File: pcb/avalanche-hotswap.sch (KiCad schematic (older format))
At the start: 83 parts, among them J1 TRRS, SW1 SW_Push, SW10 SW_Push, SW11 SW_Push, SW12 SW_Push, SW13 SW_Push, SW14 SW_Push, SW15 SW_Push, SW16 SW_Push, SW17 SW_Push, SW18 SW_Push, SW19 SW_Push, SW2 SW_Push, SW20 SW_Push, SW21 SW_Push, SW22 SW_Push, SW23 SW_Push, SW24 SW_Push, SW25 SW_Push, SW26 SW_Push, SW27 SW_Push, SW28 SW_Push, SW29 SW_Push, SW3 SW_Push, SW30 SW_Push, SW31 SW_Push, SW32 SW_Push, SW4 SW_Push, SW5 SW_Push, SW6 SW_Push, SW7 SW_Push, SW8 SW_Push, SW9 SW_Push, U1 ProMicro

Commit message: Added to schema: * OLED * LED
Imported some footprints and symbols from Lily58
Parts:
- removed JP1, JP2, JP3, JP4: Jumper, used_footprints:Jumper_SMD, symbol Jumper:Jumper_2_Bridged
- added J2: LED, symbol 123_Lily58_Pro-cache:Lily58-cache_LED
- added J3: OLED, symbol 123_Lily58_Pro-cache:Lily58-cache_OLED
- added JP1, JP2, JP3, JP4, JP5, JP6, JP7, JP8: Device_Jumper_NO_Small, symbol 123_Lily58_Pro-cache:Device_Jumper_NO_Small
- added P1, P2: i2c_pin, symbol 123_Lily58_Pro-cache:Lily58-cache_i2c_pin
- added W1: jumper, symbol 123_Lily58_Pro-cache:Device_Jumper
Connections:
- net labels added: DATA, row0, row1, row2, row3, row4, row5
- net labels removed: rowA, rowB, rowC, rowD, rowE, rowF
- wire segments 88 -> 102
- no-connect marks 5 -> 3
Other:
- moved on the sheet: HM1, HM10, HM11, HM12, HM2, HM3, HM4, HM5, HM6, HM7, HM8, HM9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

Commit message: Moved all symbols to avalanche-hotswap.lib
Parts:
- J1: symbol avalanche-hotswap-rescue:MJ-4PP-9-kbd-Pcb-rescue-jiran-classic-rescue-jiran-hotswap-rescue-jiran-hotswap-rescue-thing60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 -> avalanche-hotswap:MJ-4PP-9
- J2: symbol 123_Lily58_Pro-cache:Lily58-cache_LED -> avalanche-hotswap:LED
- J3: symbol 123_Lily58_Pro-cache:Lily58-cache_OLED -> avalanche-hotswap:OLED
- JP1, JP2, JP3, JP4, JP5, JP6, JP7, JP8: symbol 123_Lily58_Pro-cache:Device_Jumper_NO_Small -> avalanche-hotswap:Device_Jumper_NO_Small
- P1, P2: symbol 123_Lily58_Pro-cache:Lily58-cache_i2c_pin -> avalanche-hotswap:i2c_pin
- U1: symbol avalanche-hotswap-rescue:ProMicro-kbd-Pcb-rescue-jiran-classic-rescue-jiran-hotswap-rescue-jiran-hotswap-rescue-thing60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 -> avalanche-hotswap:ProMicro_2
- W1: symbol 123_Lily58_Pro-cache:Device_Jumper -> avalanche-hotswap:Device_Jumper
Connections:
- net GND: now also J1.4; no longer J1.A
- net VCC: now also J1.1; no longer J1.D
- net at P2.1 (Pin_1), W1.2: now also J1.3; no longer J1.B
- net at P1.1 (Pin_1): now also J1.2; no longer J1.C
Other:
- moved on the sheet: P1, P2, R1, R2, W1

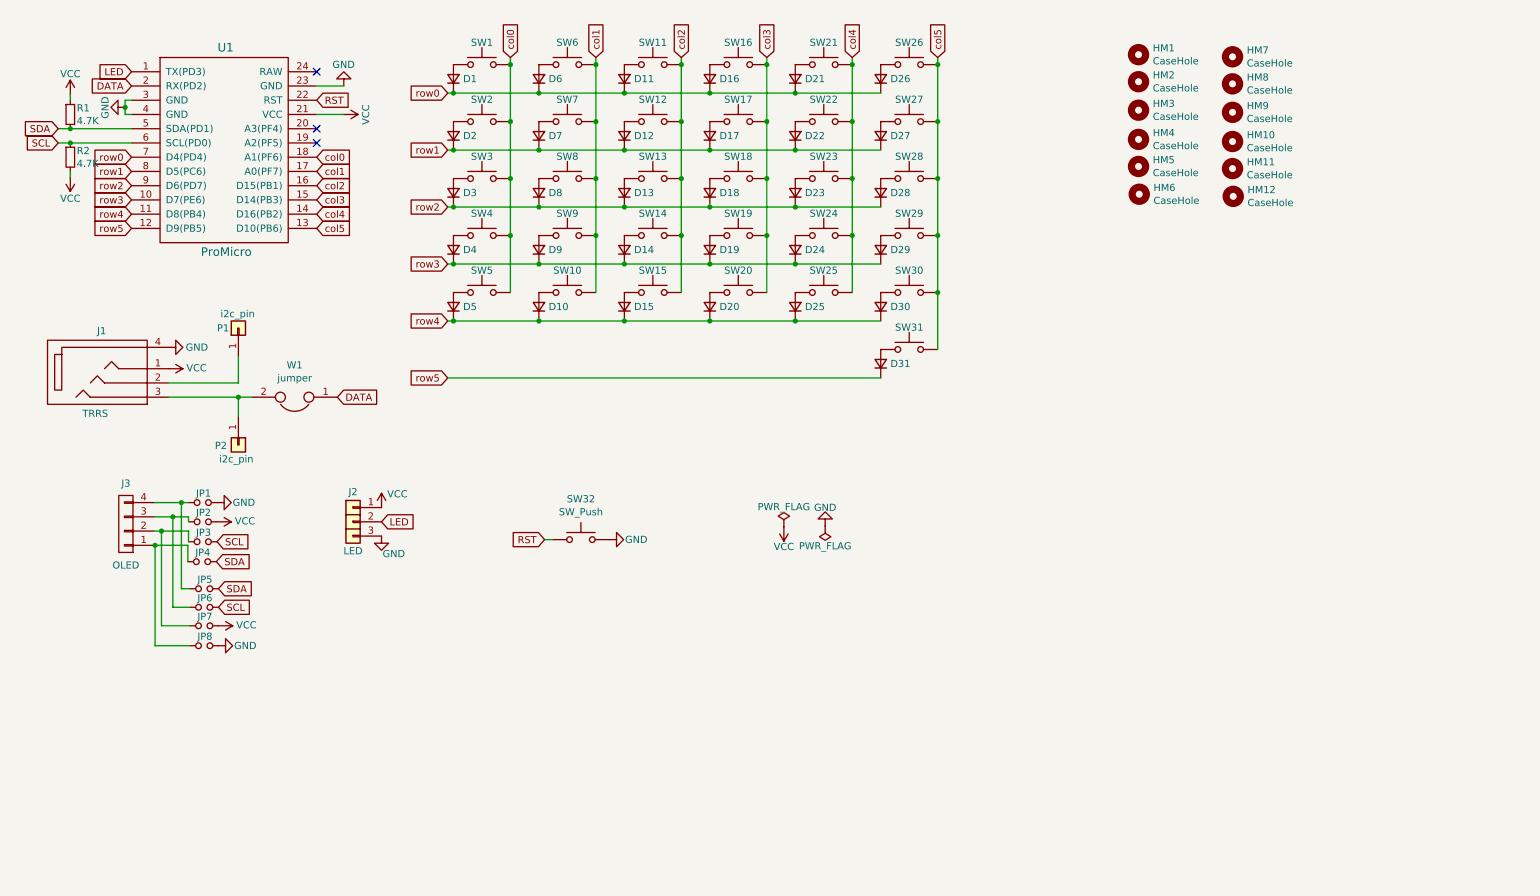
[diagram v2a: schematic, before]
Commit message: Added underglow LEDs and many more...
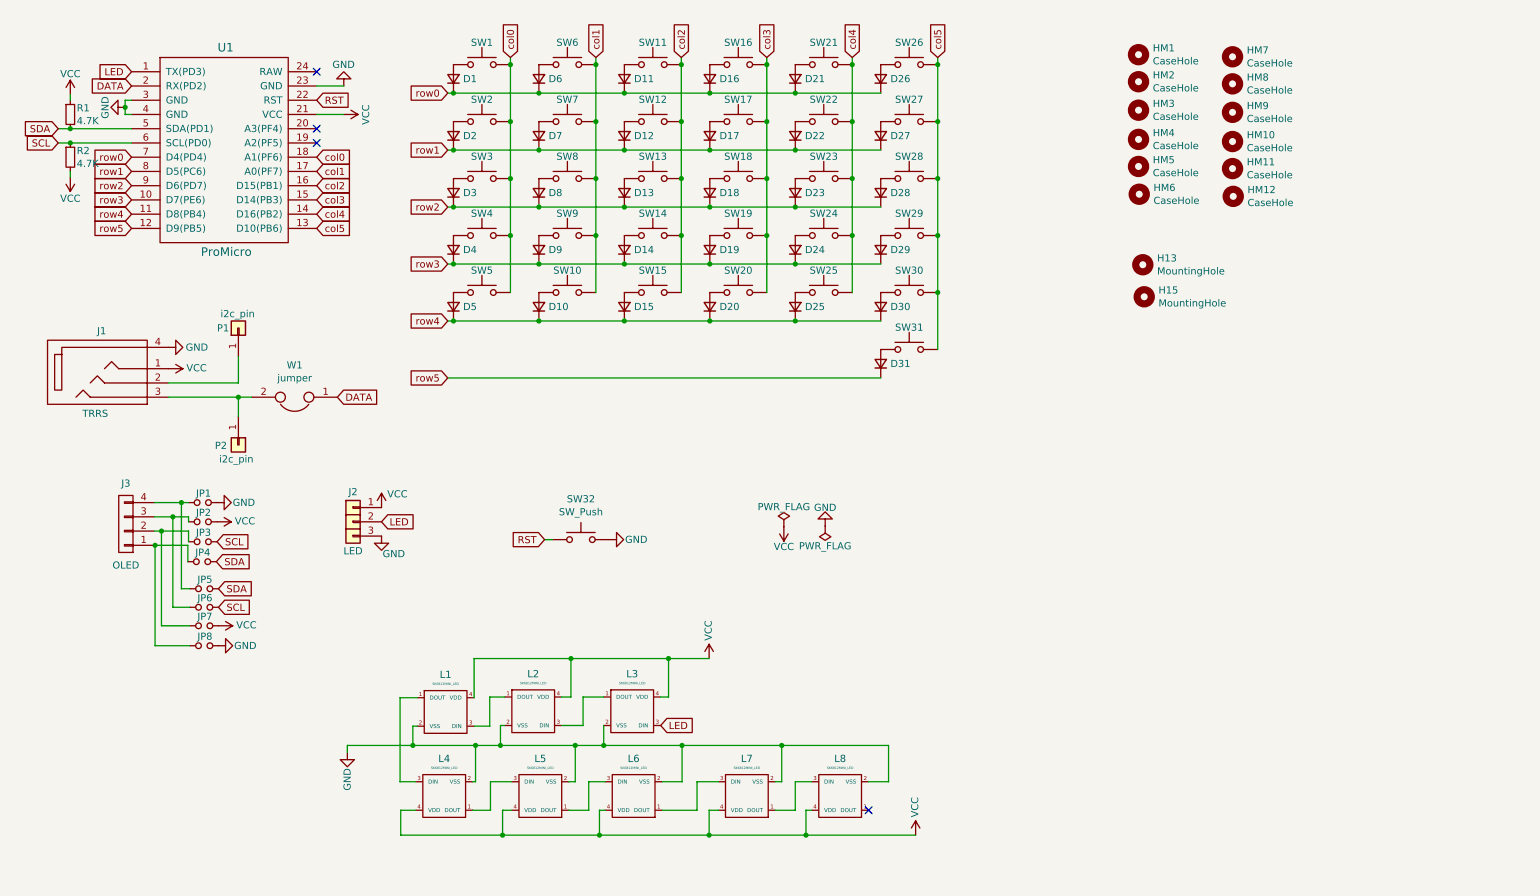
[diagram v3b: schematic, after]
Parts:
- added H13, H15: MountingHole, used_footprints:M2_HOLE_PCB, symbol Mechanical:MountingHole
- added L1, L2, L3, L4, L5, L6, L7, L8: SK6812MINI_LED, used_footprints:SK6812MINI_underglow_rev, symbol avalanche-hotswap:SK6812MINI_LED
- J1: footprint used_footprints:TRSS_DUAL_THT -> used_footprints:MJ-4PP-9
- J2: footprint (none) -> used_footprints:LED
- J3: footprint (none) -> used_footprints:OLED_4Pin
- JP1, JP2, JP3, JP4, JP5, JP6, JP7, JP8: footprint (none) -> used_footprints:avalanche_Jumper
- P1, P2: footprint (none) -> used_footprints:1pin_conn
- R1, R2: footprint used_footprints:Resistor_Hybrid_1205 -> used_footprints:RESISTOR_mini
- U1: footprint used_footprints:ProMicro_Dual -> used_footprints:ProMicro_rev2
- W1: footprint (none) -> used_footprints:jumper_data
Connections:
- net GND: now also L1.2 (VSS), L2.2 (VSS), L3.2 (VSS), L4.2 (VSS), L5.2 (VSS), L6.2 (VSS), L7.2 (VSS), L8.2 (VSS)
- net LED: now also L3.3 (DIN)
- net VCC: now also L1.4 (VDD), L2.4 (VDD), L3.4 (VDD), L4.4 (VDD), L5.4 (VDD), L6.4 (VDD), L7.4 (VDD), L8.4 (VDD)
- new net: L7.1 (DOUT), L8.3 (DIN)
- new net: L6.1 (DOUT), L7.3 (DIN)
- new net: L1.1 (DOUT), L4.3 (DIN)
- new net: L1.3 (DIN), L2.1 (DOUT)
- new net: L2.3 (DIN), L3.1 (DOUT)
- new net: L4.1 (DOUT), L5.3 (DIN)
- new net: L5.1 (DOUT), L6.3 (DIN)
- no-connect marks 3 -> 4

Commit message: WIP
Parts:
- added H16: MountingHole, used_footprints:M2_HOLE_PCB, symbol Mechanical:MountingHole
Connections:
- net at L7.1 (DOUT): now also L6.3 (DIN); no longer L8.3 (DIN)
- net at L7.3 (DIN): now also L8.1 (DOUT); no longer L6.1 (DOUT)
- net at L4.3 (DIN): now also L5.1 (DOUT); no longer L1.1 (DOUT)
- net at L4.1 (DOUT): no longer L5.3 (DIN)
- new net: L5.3 (DIN), L6.1 (DOUT)
- new net L_pin1_to_3: L1.1 (DOUT), L8.3 (DIN)
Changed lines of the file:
@@
 F 3 "" H 3480 6025 60  0001 C CNN
 	1    3480 6025
-	-1   0    0    1
+	1    0    0    -1
 $EndComp
 $Comp
@@
 F 3 "" H 4155 6025 60  0001 C CNN
 	1    4155 6025
-	-1   0    0    1
+	1    0    0    -1
 $EndComp
 $Comp
@@
 F 3 "" H 4810 6025 60  0001 C CNN
 	1    4810 6025
-	-1   0    0    1
+	1    0    0    -1
 $EndComp
 Text GLabel 5000 5530 2    50   Input ~ 0
 LED
 $Comp
-L power:VCC #PWR?
+L power:VCC #PWR0107
 U 1 1 6057DCAA
 P 5340 5060
-F 0 "#PWR?" H 5340 4910 50  0001 C CNN
+F 0 "#PWR0107" H 5340 4910 50  0001 C CNN
 F 1 "VCC" V 5335 5185 50  0000 L CNN
 F 2 "" H 5340 5060 50  0001 C CNN
@@
 	3800 5535 3690 5535
 Wire Wire Line
-	3290 5335 3170 5335
-Wire Wire Line
-	3170 5335 3170 5925
-Wire Wire Line
-	3170 5925 3280 5925
-Wire Wire Line
 	3955 5925 3805 5925
 Wire Wire Line
@@
 	4495 6125 4355 6125
 $Comp
-L power:GND #PWR?
+L power:GND #PWR0108
 U 1 1 605AF8A2
 P 2800 5720
-F 0 "#PWR?" H 2800 5470 50  0001 C CNN
+F 0 "#PWR0108" H 2800 5470 50  0001 C CNN
 F 1 "GND" V 2800 5610 50  0000 R CNN
 F 2 "" H 2800 5720 50  0001 C CNN
@@
 Connection ~ 3260 5670
 Wire Wire Line
-	3260 5670 3700 5670
-Wire Wire Line
 	3905 5530 3875 5530
 Wire Wire Line
@@
 Connection ~ 3875 5670
 Wire Wire Line
-	3875 5670 4400 5670
-Wire Wire Line
-	4600 5670 5150 5670
-Wire Wire Line
-	5150 5670 5150 5925
-Wire Wire Line
 	5150 5925 5010 5925
 Connection ~ 4600 5670
 Wire Wire Line
-	3280 6125 3175 6125
-Wire Wire Line
-	3175 6125 3175 6300
-Wire Wire Line
-	3175 6300 3890 6300
-Wire Wire Line
 	4610 6125 4570 6125
 Wire Wire Line
@@
 	3890 6300 4570 6300
 $Comp
-L power:VCC #PWR?
+L power:VCC #PWR0109
 U 1 1 6061C798
-P 6790 6300
-F 0 "#PWR?" H 6790 6150 50  0001 C CNN
-F 1 "VCC" V 6785 6425 50  0000 L CNN
-F 2 "" H 6790 6300 50  0001 C CNN
-F 3 "" H 6790 6300 50  0001 C CNN
-	1    6790 6300
+P 6990 5780
+F 0 "#PWR0109" H 6990 5630 50  0001 C CNN
+F 1 "VCC" V 6985 5905 50  0000 L CNN
+F 2 "" H 6990 5780 50  0001 C CNN
+F 3 "" H 6990 5780 50  0001 C CNN
+	1    6990 5780
 	1    0    0    -1
 $EndComp
@@
 	3680 5925 3700 5925
 Wire Wire Line
-	3700 5925 3700 5670
-Connection ~ 3700 5670
-Wire Wire Line
-	3700 5670 3875 5670
-Wire Wire Line
 	4355 5925 4400 5925
-Wire Wire Line
-	4400 5925 4400 5670
-Connection ~ 4400 5670
-Wire Wire Line
-	4400 5670 4600 5670
 $Comp
 L avalanche-hotswap:SK6812MINI_LED L7
@@
 F 3 "" H 5605 6025 60  0001 C CNN
 	1    5605 6025
-	-1   0    0    1
+	1    0    0    -1
 $EndComp
 $Comp
@@
 F 3 "" H 6260 6025 60  0001 C CNN
 	1    6260 6025
-	-1   0    0    1
+	1    0    0    -1
 $EndComp
 Wire Wire Line
@@
 	5945 6125 5805 6125
 Wire Wire Line
-	6600 5925 6460 5925
-Wire Wire Line
 	6060 6125 6020 6125
 Wire Wire Line
 	6020 6125 6020 6300
-Connection ~ 6020 6300
-Wire Wire Line
-	6020 6300 6790 6300
 Wire Wire Line
 	5405 6125 5340 6125
-NoConn ~ 6460 6125
 Wire Wire Line
 	5805 5925 5850 5925
-Wire Wire Line
-	5850 5925 5850 5670
 Wire Wire Line
 	4570 6300 5340 6300
@@
 Wire Wire Line
 	5340 6300 6020 6300
-Wire Wire Line
-	5850 5670 5150 5670
-Connection ~ 5150 5670
-Wire Wire Line
-	6600 5925 6600 5670
-Wire Wire Line
-	6600 5670 5850 5670
-Connection ~ 5850 5670
+$Comp
+L power:GND #PWR0110
+U 1 1 60493A43
+P 2715 6350
+F 0 "#PWR0110" H 2715 6100 50  0001 C CNN
+F 1 "GND" V 2715 6240 50  0000 R CNN
+F 2 "" H 2715 6350 50  0001 C CNN
+F 3 "" H 2715 6350 50  0001 C CNN
+	1    2715 6350
+	1    0    0    -1
+$EndComp
+Wire Wire Line
+	2715 6350 2715 6300
+Wire Wire Line
+	2715 6300 3170 6300
+Wire Wire Line
+	3260 5670 3875 5670
+Wire Wire Line
+	3875 5670 4600 5670
+Wire Wire Line
+	4600 5670 6600 5670
+Wire Wire Line
+	6460 5925 6535 5925
+Wire Wire Line
+	6535 5925 6535 5780
+Connection ~ 6535 5780
+Wire Wire Line
+	6535 5780 6990 5780
+Wire Wire Line
+	5850 5780 5850 5925
+Wire Wire Line
+	5850 5780 6535 5780
+Wire Wire Line
+	5850 5780 5150 5780
+Wire Wire Line
+	5150 5780 5150 5925
+Connection ~ 5850 5780
+Wire Wire Line
+	5150 5780 4400 5780
+Wire Wire Line
+	4400 5780 4400 5925
+Connection ~ 5150 5780
+Wire Wire Line
+	4400 5780 3700 5780
+Wire Wire Line
+	3700 5780 3700 5925
+Connection ~ 4400 5780
+Wire Wire Line
+	3280 6125 3170 6125
+Wire Wire Line
+	3170 6125 3170 6300
+Connection ~ 3170 6300
+Wire Wire Line
+	3170 6300 3890 6300
+NoConn ~ 3280 5925
+Text Label 3290 5335 2    50   ~ 0
+L_pin1_to_3
+Text Label 6460 6125 0    50   ~ 0
+L_pin1_to_3
+$Comp
+L Mechanical:MountingHole H16
+U 1 1 6044455C
+P 8415 2760
+F 0 "H16" H 8515 2806 50  0000 L CNN
+F 1 "MountingHole" H 8515 2715 50  0000 L CNN
+F 2 "used_footprints:M2_HOLE_PCB" H 8415 2760 50  0001 C CNN
+F 3 "~" H 8415 2760 50  0001 C CNN
+	1    8415 2760
+	1    0    0    -1
+$EndComp
 $EndSCHEMATC

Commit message: Routing...
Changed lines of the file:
@@
 Wire Wire Line
 	5150 5925 5010 5925
-Connection ~ 4600 5670
 Wire Wire Line
 	4610 6125 4570 6125
@@
 	3875 5670 4600 5670
 Wire Wire Line
-	4600 5670 6600 5670
-Wire Wire Line
 	6460 5925 6535 5925

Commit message: Routing...
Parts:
- renumbered L3 to L1, L1 to L3, L8 to L4, L7 to L5, L5 to L7, L4 to L8
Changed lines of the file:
@@
 $EndComp
 $Comp
-L avalanche-hotswap:SK6812MINI_LED L1
+L avalanche-hotswap:SK6812MINI_LED L3
 U 1 1 60550286
 P 3490 5435
-F 0 "L1" H 3490 5697 51  0000 C CNN
+F 0 "L3" H 3490 5697 51  0000 C CNN
 F 1 "SK6812MINI_LED" H 3490 5632 16  0000 C CNN
 F 2 "used_footprints:SK6812MINI_underglow_rev" H 3490 5435 60  0001 C CNN
@@
 $EndComp
 $Comp
-L avalanche-hotswap:SK6812MINI_LED L3
+L avalanche-hotswap:SK6812MINI_LED L1
 U 1 1 605637A3
 P 4800 5430
-F 0 "L3" H 4800 5692 51  0000 C CNN
+F 0 "L1" H 4800 5692 51  0000 C CNN
 F 1 "SK6812MINI_LED" H 4800 5627 16  0000 C CNN
 F 2 "used_footprints:SK6812MINI_underglow_rev" H 4800 5430 60  0001 C CNN
@@
 $EndComp
 $Comp
-L avalanche-hotswap:SK6812MINI_LED L4
+L avalanche-hotswap:SK6812MINI_LED L8
 U 1 1 60567077
 P 3480 6025
-F 0 "L4" H 3480 5763 51  0000 C CNN
+F 0 "L8" H 3480 5763 51  0000 C CNN
 F 1 "SK6812MINI_LED" H 3480 5828 16  0000 C CNN
 F 2 "used_footprints:SK6812MINI_underglow_rev" H 3480 6025 60  0001 C CNN
@@
 $EndComp
 $Comp
-L avalanche-hotswap:SK6812MINI_LED L5
+L avalanche-hotswap:SK6812MINI_LED L7
 U 1 1 6056A5E2
 P 4155 6025
-F 0 "L5" H 4155 5763 51  0000 C CNN
+F 0 "L7" H 4155 5763 51  0000 C CNN
 F 1 "SK6812MINI_LED" H 4155 5828 16  0000 C CNN
 F 2 "used_footprints:SK6812MINI_underglow_rev" H 4155 6025 60  0001 C CNN
@@
 	4355 5925 4400 5925
 $Comp
-L avalanche-hotswap:SK6812MINI_LED L7
+L avalanche-hotswap:SK6812MINI_LED L5
 U 1 1 60436647
 P 5605 6025
-F 0 "L7" H 5605 5763 51  0000 C CNN
+F 0 "L5" H 5605 5763 51  0000 C CNN
 F 1 "SK6812MINI_LED" H 5605 5828 16  0000 C CNN
 F 2 "used_footprints:SK6812MINI_underglow_rev" H 5605 6025 60  0001 C CNN
@@
 $EndComp
 $Comp
-L avalanche-hotswap:SK6812MINI_LED L8
+L avalanche-hotswap:SK6812MINI_LED L4
 U 1 1 6043664D
 P 6260 6025
-F 0 "L8" H 6260 5763 51  0000 C CNN
+F 0 "L4" H 6260 5763 51  0000 C CNN
 F 1 "SK6812MINI_LED" H 6260 5828 16  0000 C CNN
 F 2 "used_footprints:SK6812MINI_underglow_rev" H 6260 6025 60  0001 C CNN
